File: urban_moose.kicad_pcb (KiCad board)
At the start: 2 copper layers, 27.4 x 49.5 mm, 52 parts, among them P1 SWD, P2 EXT, P3 ANT, Q1 MOSFET_N, Q2 MOSFET_N, SW1 SW_PUSH, U1 nRF51822-QFAA, U2 DS18B20, U3 BMP180, U4 Si1145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

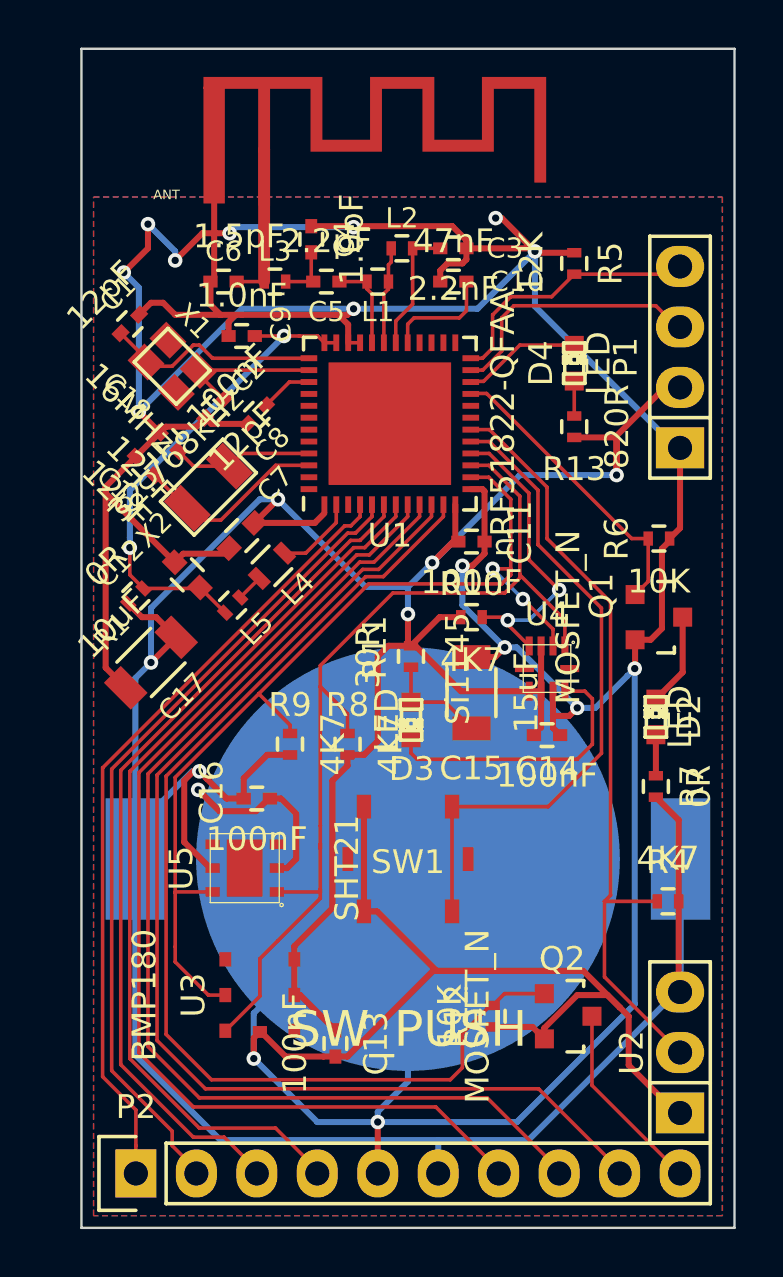
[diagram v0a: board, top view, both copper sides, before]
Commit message: Fixes to match library changes
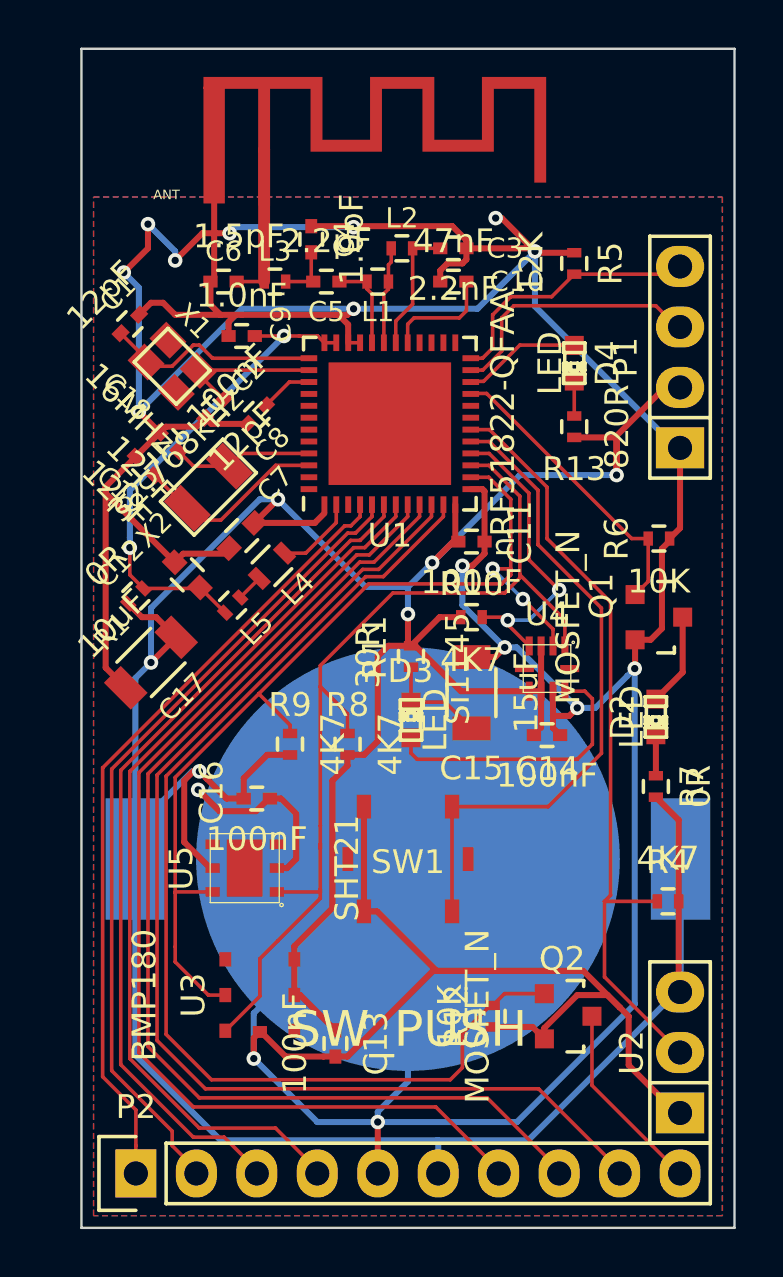
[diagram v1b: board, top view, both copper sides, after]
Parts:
- turned D2 to 270 degrees
- turned D3 to 90 degrees
- turned D4 to 270 degrees
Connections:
- D3 pad 1: Net-(C15-Pad1) -> Net-(D3-Pad1)
- D3 pad 2: Net-(D3-Pad2) -> Net-(C15-Pad1)
- D4 pad 1: Net-(D4-Pad1) -> LED
- D4 pad 2: LED -> Net-(D4-Pad2)
- Q1 pad 3: Net-(D2-Pad2) -> Net-(D2-Pad1)
- R13 pad 2: Net-(D4-Pad1) -> Net-(D4-Pad2)
- R7 pad 2: Net-(D2-Pad1) -> Net-(D2-Pad2)
- U1 pad 19: Net-(U1-Pad19) -> (no net)
- U1 pad 20: Net-(U1-Pad20) -> (no net)
- U1 pad 25: Net-(U1-Pad25) -> (no net)
- U1 pad 26: Net-(U1-Pad26) -> (no net)
- U1 pad 27: Net-(U1-Pad27) -> (no net)
- U1 pad 28: Net-(U1-Pad28) -> (no net)
- U1 pad 3: Net-(U1-Pad3) -> (no net)
- U1 pad 40: Net-(U1-Pad40) -> (no net)
- U1 pad 41: Net-(U1-Pad41) -> (no net)
- U1 pad 42: Net-(U1-Pad42) -> (no net)
- U1 pad 43: Net-(U1-Pad43) -> (no net)
- U1 pad 44: Net-(U1-Pad44) -> (no net)
- U1 pad 47: Net-(U1-Pad47) -> (no net)
- U1 pad 48: Net-(U1-Pad48) -> (no net)
- U3 pad 1: Net-(U3-Pad1) -> (no net)
- U3 pad 4: Net-(U3-Pad4) -> (no net)
- U4 pad 10: Net-(U4-Pad10) -> (no net)
- U4 pad 5: Net-(U4-Pad5) -> (no net)
- U4 pad 9: Net-(D3-Pad2) -> Net-(D3-Pad1)
- U5 pad 3: Net-(U5-Pad3) -> (no net)
- U5 pad 4: Net-(U5-Pad4) -> (no net)
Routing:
- net Net-(D3-Pad2): track 11.8 -> 0.00 mm
- net Net-(D3-Pad1): track 0.00 -> 11.8 mm
- net Net-(D2-Pad2): track 3.91 -> 1.72 mm
- net Net-(D2-Pad1): track 1.72 -> 3.91 mm
- net Net-(D4-Pad2): track 0.00 -> 1.47 mm
- net Net-(D4-Pad1): track 1.47 -> 0.00 mm

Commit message: Change footprint for nRF51 to the correct pitch
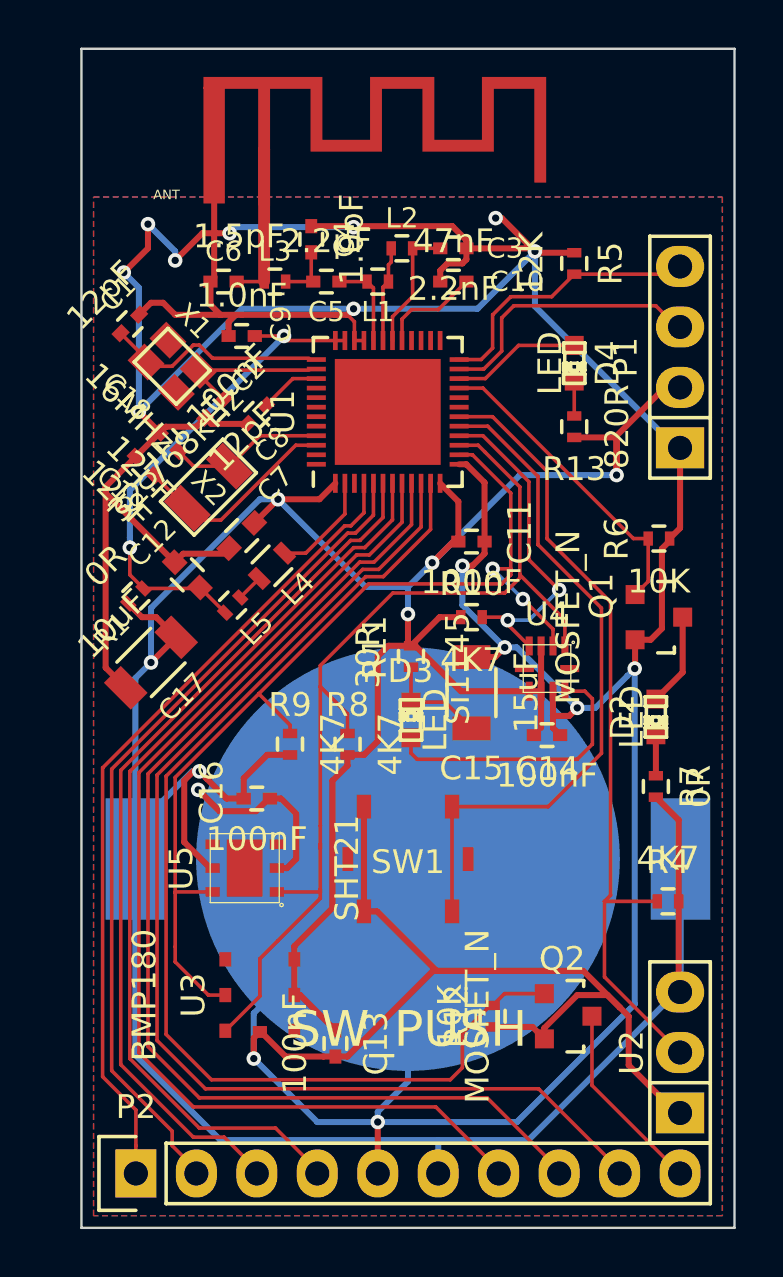
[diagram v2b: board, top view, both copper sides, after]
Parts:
- U1: footprint Housings_DFN_QFN:QFN-48-1EP_7x7mm_Pitch0.5mm -> Housings_DFN_QFN:UQFN-48-1EP_6x6mm_Pitch0.4mm
- moved U1 0.50 mm to (145.2, 91.2)
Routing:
- net SWITCH: track 27.4 -> 28.5 mm
- net SI1145_INT: track 13.0 -> 14.1 mm
- net SDA: track 41.3 -> 42.3 mm
- net AREF0: track 33.3 -> 34.4 mm
- net Net-(L4-Pad1): track 3.46 -> 4.51 mm
- net AIN4: track 38.1 -> 39.2 mm
- net SCL: track 42.2 -> 43.2 mm
- net DS18B20: track 33.5 -> 34.5 mm
- net AIN6: track 47.4 -> 48.4 mm
- net AIN5: track 45.3 -> 46.2 mm
- net AIN3: track 36.0 -> 36.9 mm
- net FET1: track 46.5 -> 47.4 mm
- net AIN7: track 49.5 -> 50.3 mm
- net GND: track 257.5 -> 258.3 mm
- net AIN2: track 34.3 -> 35.0 mm
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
